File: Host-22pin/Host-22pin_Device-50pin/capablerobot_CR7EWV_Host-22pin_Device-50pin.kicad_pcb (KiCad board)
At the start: 2 copper layers, 25.5 x 99.8 mm, 2 parts, among them J1 WE_687622100002_FLEX, J2 WE_687650100002_FLEX

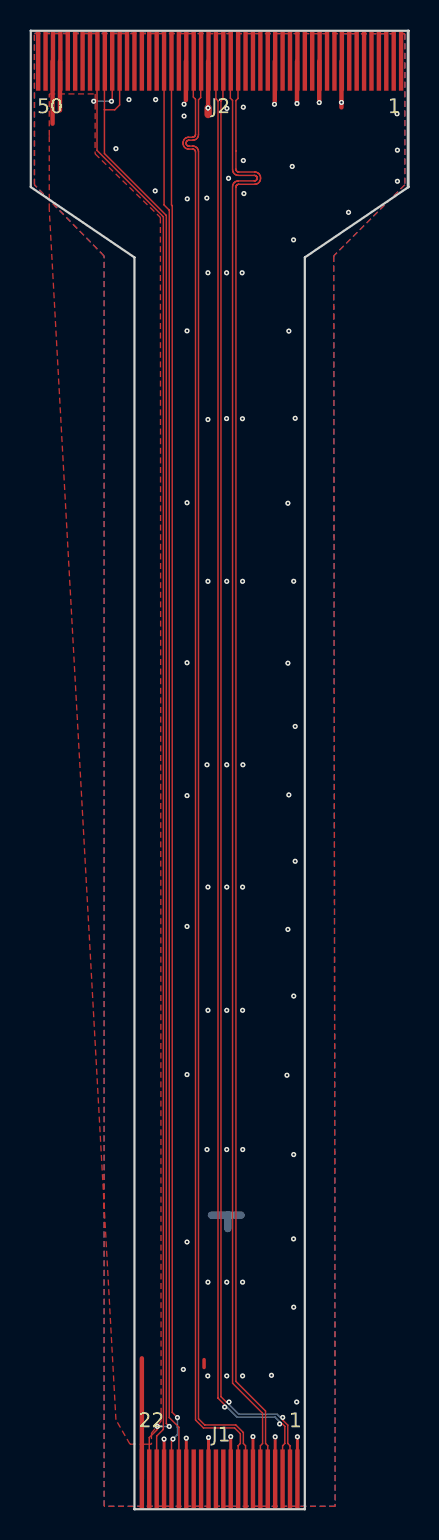
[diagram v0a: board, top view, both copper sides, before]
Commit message: Change 22 pin to 4 lane interface and change 15 pin and 22 pin to alternate MIPI interface
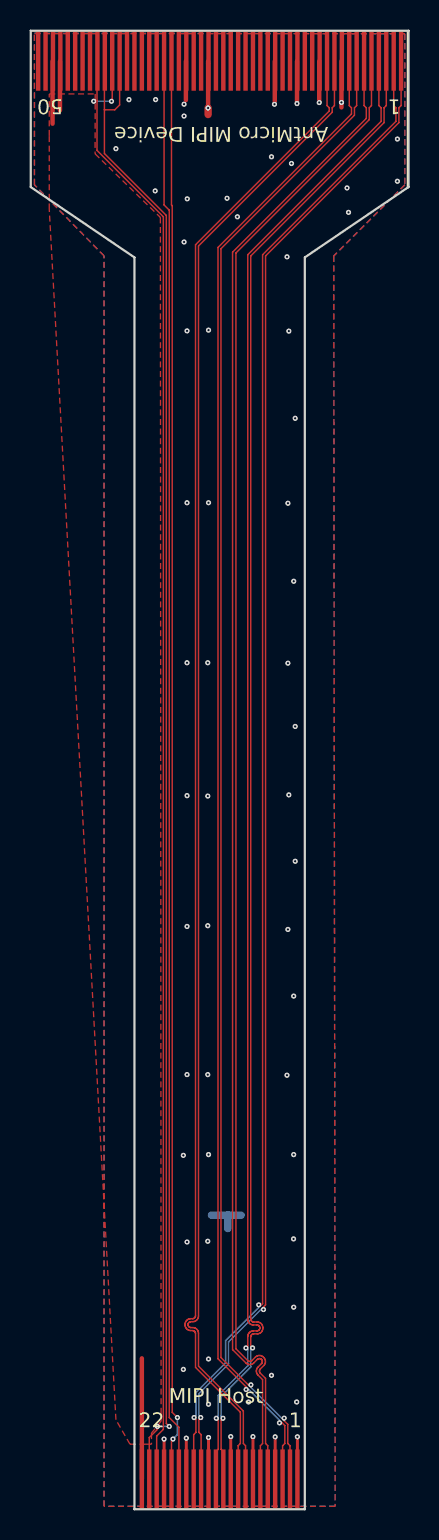
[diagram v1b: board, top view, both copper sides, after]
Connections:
- J1 pad 11: Net-(J1-Pad11) -> /CSI0_D2_N
- J1 pad 12: Net-(J1-Pad12) -> /CSI0_D2_P
- J1 pad 14: Net-(J1-Pad14) -> /CSI0_D3_N
- J1 pad 15: Net-(J1-Pad15) -> /CSI0_D3_P
- J2 pad 1: Net-(J2-Pad1) -> /CSI0_D3_N
- J2 pad 10: Net-(J2-Pad10) -> /CSI0_CLK_N
- J2 pad 11: Net-(J2-Pad11) -> /CSI0_CLK_P
- J2 pad 13: Net-(J2-Pad13) -> (no net)
- J2 pad 14: Net-(J2-Pad14) -> (no net)
- J2 pad 16: Net-(J2-Pad16) -> (no net)
- J2 pad 17: Net-(J2-Pad17) -> (no net)
- J2 pad 19: Net-(J2-Pad19) -> (no net)
- J2 pad 2: Net-(J2-Pad2) -> /CSI0_D3_P
- J2 pad 20: Net-(J2-Pad20) -> (no net)
- J2 pad 21: Net-(J2-Pad21) -> (no net)
- J2 pad 22: Net-(J2-Pad22) -> (no net)
- J2 pad 23: /CSI0_D1_N -> (no net)
- J2 pad 24: /CSI0_D1_P -> (no net)
- J2 pad 25: /CSI0_D0_N -> (no net)
- J2 pad 26: /CSI0_D0_P -> (no net)
- J2 pad 28: /CSI0_CLK_N -> (no net)
- J2 pad 29: /CSI0_CLK_P -> (no net)
- J2 pad 3: Net-(J2-Pad3) -> /CSI0_D2_N
- J2 pad 31: Net-(J2-Pad31) -> (no net)
- J2 pad 34: Net-(J2-Pad34) -> (no net)
- J2 pad 35: Net-(J2-Pad35) -> (no net)
- J2 pad 36: Net-(J2-Pad36) -> (no net)
- J2 pad 37: Net-(J2-Pad37) -> (no net)
- J2 pad 38: Net-(J2-Pad38) -> (no net)
- J2 pad 4: Net-(J2-Pad4) -> /CSI0_D2_P
- J2 pad 43: Net-(J2-Pad43) -> (no net)
- J2 pad 44: Net-(J2-Pad44) -> (no net)
- J2 pad 45: Net-(J2-Pad45) -> (no net)
- J2 pad 46: Net-(J2-Pad46) -> (no net)
- J2 pad 49: Net-(J2-Pad49) -> (no net)
- J2 pad 5: Net-(J2-Pad5) -> /CSI0_D1_N
- J2 pad 50: Net-(J2-Pad50) -> (no net)
- J2 pad 6: Net-(J2-Pad6) -> /CSI0_D1_P
- J2 pad 7: Net-(J2-Pad7) -> /CSI0_D0_N
- J2 pad 8: Net-(J2-Pad8) -> /CSI0_D0_P
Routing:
- net /CSI0_D2_P: track 0.00 -> 101.7 mm, vias 0 -> 2
- net /CSI0_D2_N: track 0.00 -> 101.7 mm, vias 0 -> 2
- net /CSI0_D3_N: track 0.00 -> 101.6 mm, vias 0 -> 2
- net /CSI0_D3_P: track 0.00 -> 101.6 mm, vias 0 -> 2
- net /CSI0_CLK_P: track 99.5 -> 101.7 mm
- net /CSI0_CLK_N: track 99.5 -> 101.7 mm
- net /CSI0_D1_P: track 99.5 -> 101.7 mm
- net /CSI0_D0_N: track 99.4 -> 101.6 mm
- net /CSI0_D1_N: track 99.5 -> 101.7 mm
- net /CSI0_D0_P: track 99.4 -> 101.6 mm
- net /GND: track 40.6 -> 40.0 mm, vias 81 -> 64
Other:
- board text added: "AntMicro MIPI Device"
- board text added: "Capable Robot Components Inc [CRJ7RW.1] Flex Cable - CSI - 50 pin Device to 22 pin Host 100mm, same side contacts, 4 lane"
- board text added: "MIPI Host"
- board text removed: "Capable Robot Components Inc [CR7EWV] Flex Cable - CSI - 50 pin Device to 22 pin Host 100mm, same side contacts"
